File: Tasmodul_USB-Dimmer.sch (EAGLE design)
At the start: 27 parts, among them IC1 REG1117, J2 61400416021, Q1 BC817-16SMD, Q2 5.8A/30V/35mΩ, X1 USB-A

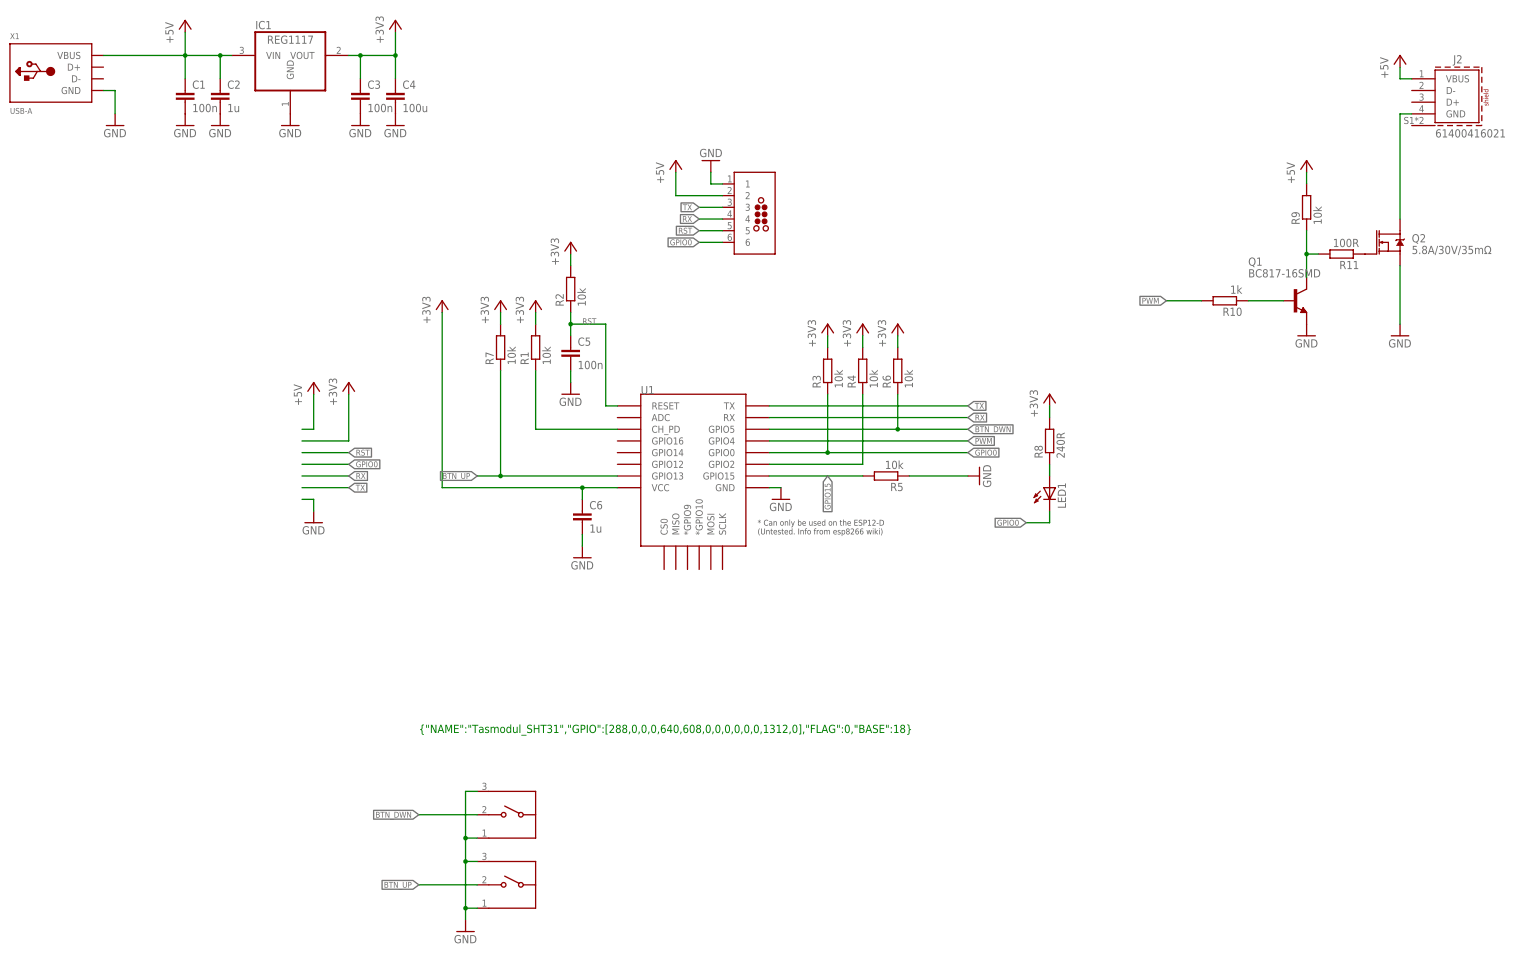
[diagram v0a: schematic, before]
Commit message: Cleaned up schematic Added SCH and GERBER Updated documentation
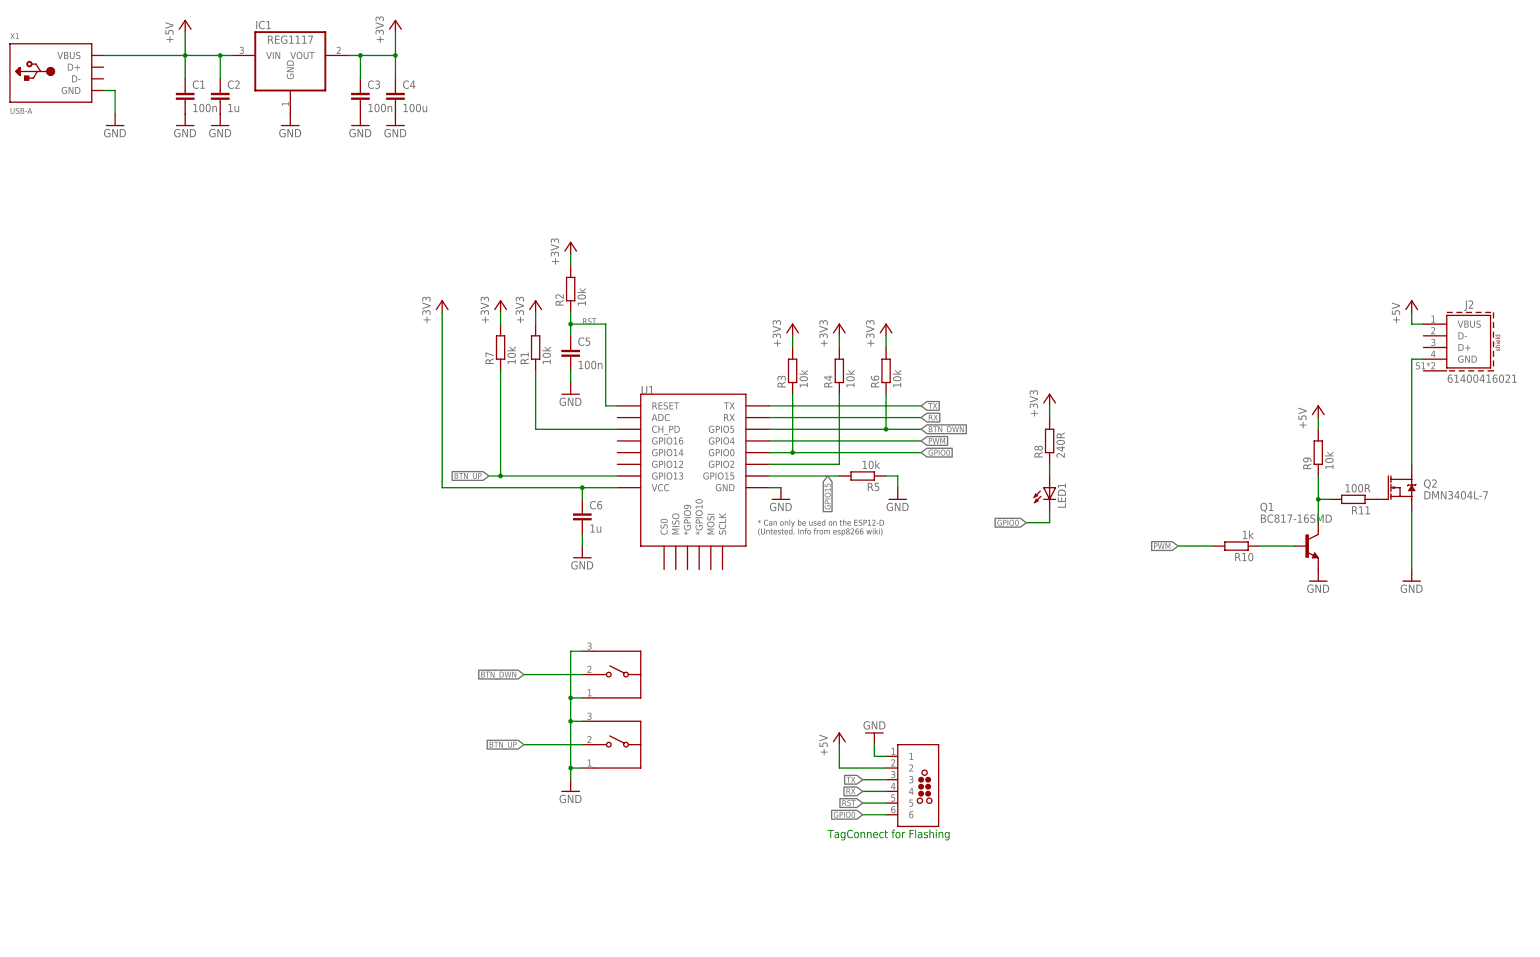
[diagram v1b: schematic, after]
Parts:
- Q2: value 5.8A/30V/35mΩ -> DMN3404L-7
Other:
- note added: "TagConnect for Flashing"
- note removed: "{"NAME":"Tasmodul_SHT31","GPIO":[288,0,0,0,640,608,0,0,0,0,0,0,1312,0],"FLAG":0,"BASE":18}"
- moved on the sheet: J2, Q1, Q2, R10, R11, R3, R4, R5, R6, R9
